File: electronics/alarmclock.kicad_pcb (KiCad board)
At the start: 2 copper layers, 100.3 x 69.9 mm, 41 parts, among them J1 Conn_01x02, J2 SWD, J3 SocketTop, J4 SocketBottem, J5 Conn_01x02, J6 Conn_01x05, J7 Conn_01x05, J8 RotaryEncoder, Q1 Backpower, SW2 Reset, U1 STM32L031F6P6, U2 74HCT595, U3 74HCT595, U4 AP2111H-3.3, Y1 24MHz

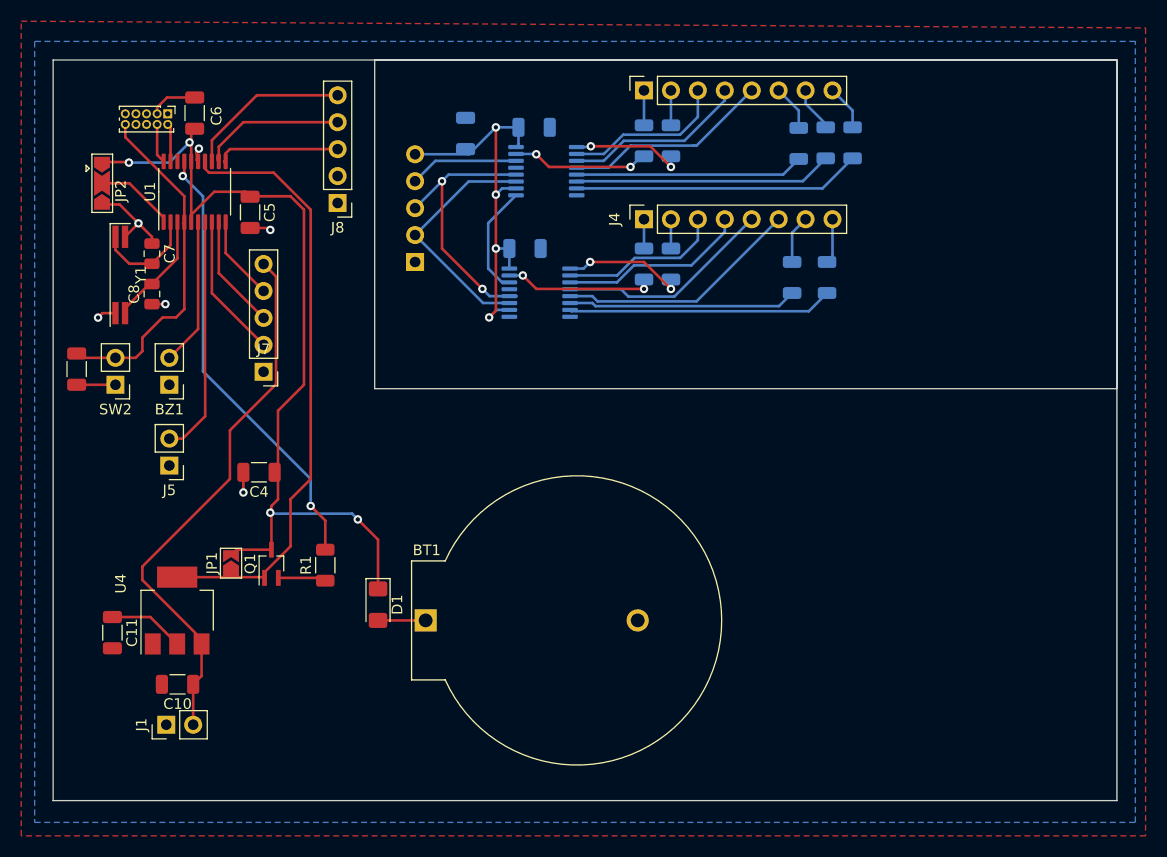
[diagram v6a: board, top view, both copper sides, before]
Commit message: Changed the pcblayout after learning more about ground
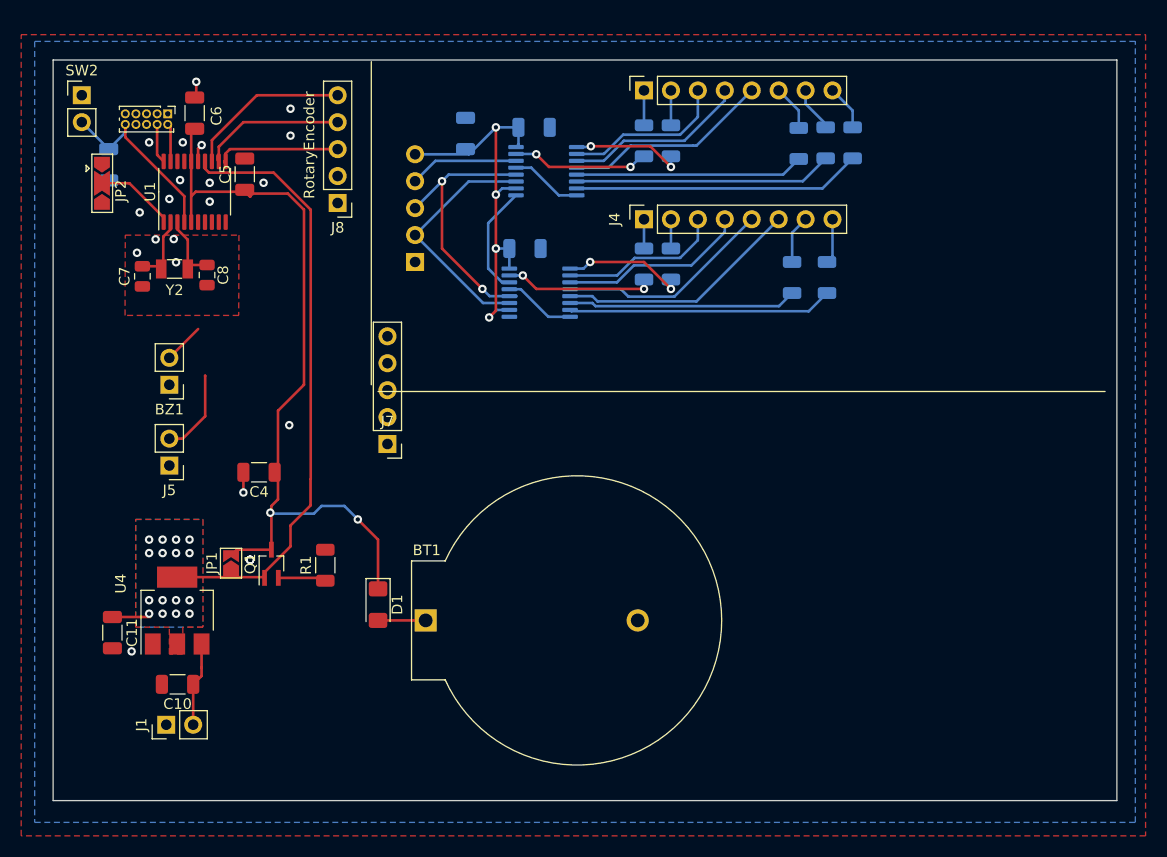
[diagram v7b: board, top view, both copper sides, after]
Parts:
- removed Y1: 24MHz, Crystal:Crystal_SMD_SeikoEpson_MC146-4Pin_6.7x1.5mm_HandSoldering
- added Y2: 32.768khz, Crystal:Crystal_SMD_3215-2Pin_3.2x1.5mm, F.Cu at (69.1, 99.6)
- C9: moved to B.Cu
- moved SW2 27.5 mm to (60.3, 83.2), turned to 0 degrees
- moved C9 19.5 mm to (62.9, 89.7)
- moved J7 13.5 mm to (89.2, 116.1)
- moved C8 5.50 mm to (72.1, 100.1)
- moved C5 3.64 mm to (75.7, 90.6), turned to 90 degrees
- moved C7 2.32 mm to (66.0, 100.3), turned to 90 degrees
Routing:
- net +5V: track 90.2 -> 46.8 mm
- net Vbat_enable: track 42.2 -> 0.00 mm, vias 2 -> 0
- net NRST: track 32.9 -> 18.1 mm
- net Mute_button: track 22.6 -> 8.09 mm
- net SRCLK: track 13.6 -> 0.00 mm
- net RCLK: track 10.8 -> 0.00 mm
- net Alarm: track 13.9 -> 3.84 mm
- net +BATT: track 84.7 -> 75.7 mm, vias 4 -> 2
- net SHIFT_IN: track 7.98 -> 0.00 mm
- net GND: track 25.4 -> 20.3 mm, vias 6 -> 22
- net OSC_OUT: track 10.8 -> 6.80 mm
- net +3.3V: track 64.2 -> 60.6 mm, vias 0 -> 16
- net OSC_IN: track 9.87 -> 6.67 mm
- added copper zone on B.Cu, net +3.3V
- added copper zone on F.Cu, net +3.3V
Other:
- outline, holes or cut-outs redrawn

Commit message: tape out
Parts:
- removed C7, C8: 12pF, Capacitor_SMD:C_0805_2012Metric
- removed Y2: 32.768khz, Crystal:Crystal_SMD_3215-2Pin_3.2x1.5mm
- added F1: Polyfuse, Fuse:Fuse_1206_3216Metric, F.Cu at (67.4, 143.5)
- added X2: ECS-327TXO-33-TR, clockcyrstal:ECS-327_ECS, F.Cu at (67.3, 98.7)
- JP2: value SolderJumper_BOOT0 -> Jumper_BOOT0
- moved J7 14.9 mm to (78.7, 105.4)
- moved J1 7.00 mm to (62.2, 146.1), turned to 180 degrees
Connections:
- J1 pad 2: +5V -> Net-(J1-Pin_2)
- U1 pad 3: OSC_OUT -> unconnected-(U1-PC15-Pad3)
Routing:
- net +5V: track 46.8 -> 116.4 mm
- net Vbat_enable: track 0.00 -> 46.3 mm, vias 0 -> 2
- net +BATT: track 75.7 -> 95.7 mm
- net Mute_button: track 8.09 -> 22.6 mm
- net SRCLK: track 0.00 -> 10.3 mm
- net Alarm: track 3.84 -> 13.9 mm
- net RCLK: track 0.00 -> 8.07 mm
- net OSC_OUT: track 6.80 -> 0.00 mm
- net SHIFT_IN: track 0.00 -> 5.94 mm
- net OSC_IN: track 6.67 -> 2.69 mm
- net Net-(J1-Pin_2): track 0.00 -> 3.81 mm
- net GND: track 20.3 -> 20.0 mm, vias 22 -> 16
- net NRST: track 18.1 -> 17.9 mm, vias 0 -> 1
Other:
- board text added: "Alarmclock Revision V1"
- board text added: "JLCJLCJLCJLC"
